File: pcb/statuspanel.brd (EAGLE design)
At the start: 57.1 x 66 mm, 3 parts

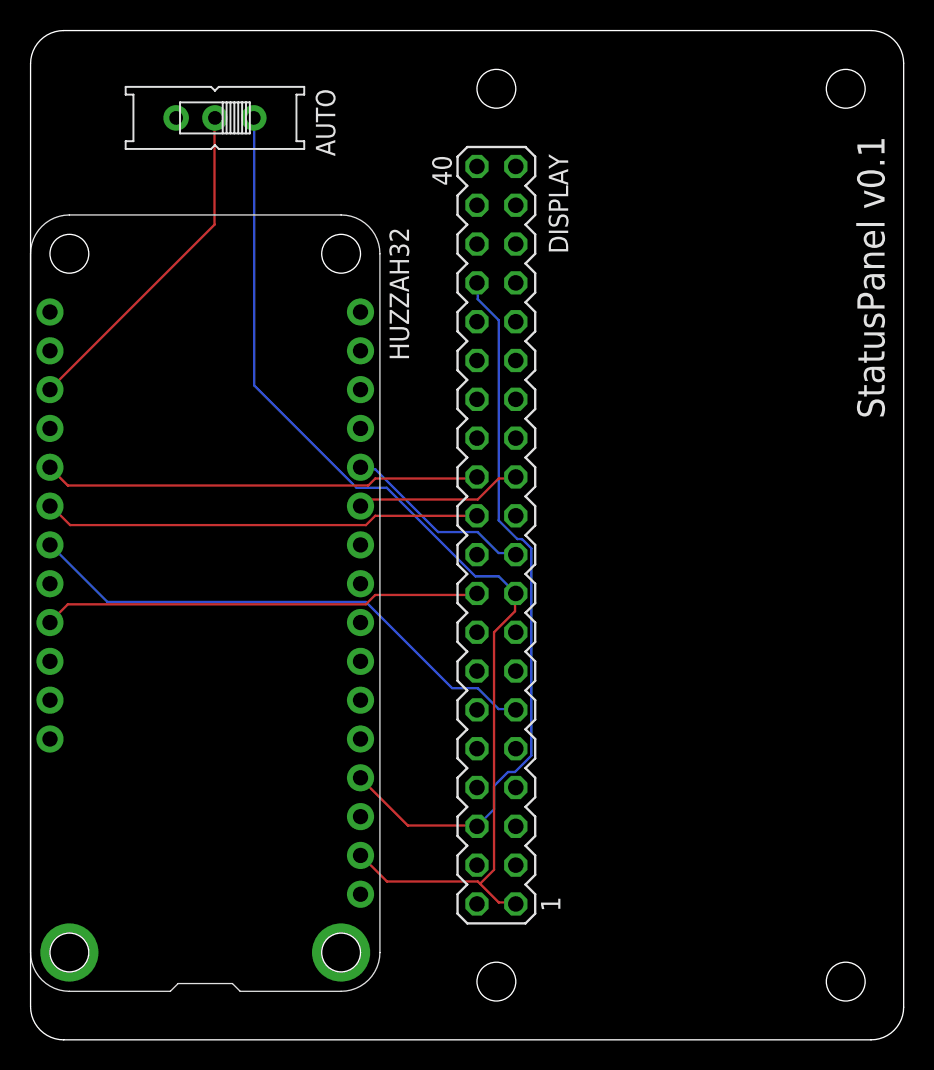
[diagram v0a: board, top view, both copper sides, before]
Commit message: Update the PCB to add an unpair button
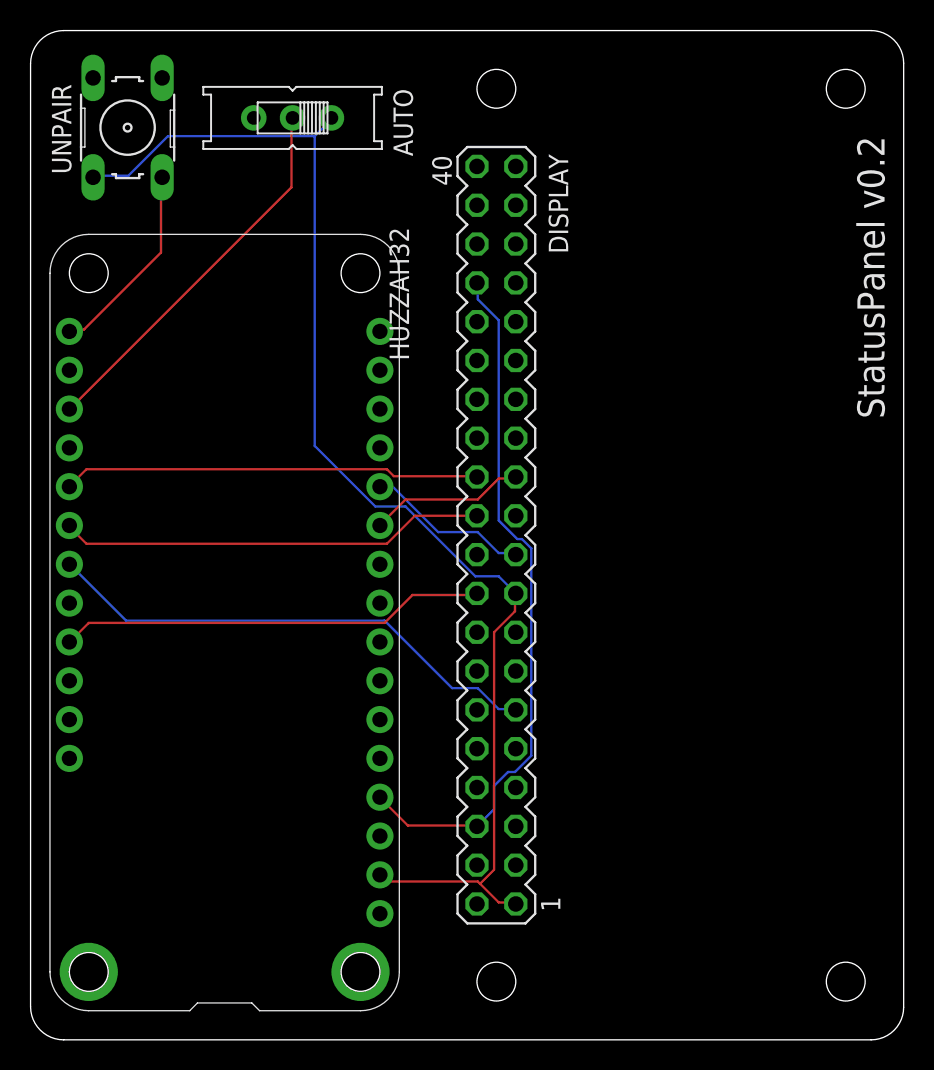
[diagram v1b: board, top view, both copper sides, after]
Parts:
- added UNPAIR: (no value), switch-omron:B3F-10XX
- moved AUTO 5.08 mm to (17.1, 60.3)
- moved HUZZAH32 1.80 mm to (24.1, 1.91)
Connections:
- new net UNPAIR: HUZZAH32.17, UNPAIR.3
- net 3V3: now also UNPAIR.1
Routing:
- net UNPAIR: track 0.00 -> 13.1 mm
- net 3V3: track 71.7 -> 84.5 mm
- net AUTO: track 22.2 -> 25.1 mm
- net RST: track 34.9 -> 33.2 mm
- net GND: track 47.9 -> 46.1 mm
- net MOSI: track 12.6 -> 10.8 mm
- net CS: track 28.7 -> 27.4 mm
- net SCLK: track 11.0 -> 10.2 mm
- net BUSY: track 28.7 -> 28.0 mm
- net DC: track 28.7 -> 28.0 mm
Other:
- board text added: "StatusPanel v0.2"
- board text removed: "StatusPanel v0.1"

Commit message: Rename RST to PANELRESET
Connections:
- net RST renamed PANELRESET
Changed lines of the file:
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@@
 </elements>
 <signals>
-<signal name="RST">
+<signal name="PANELRESET">
 <contactref element="DISPLAY" pad="11"/>
 <contactref element="HUZZAH32" pad="23"/>

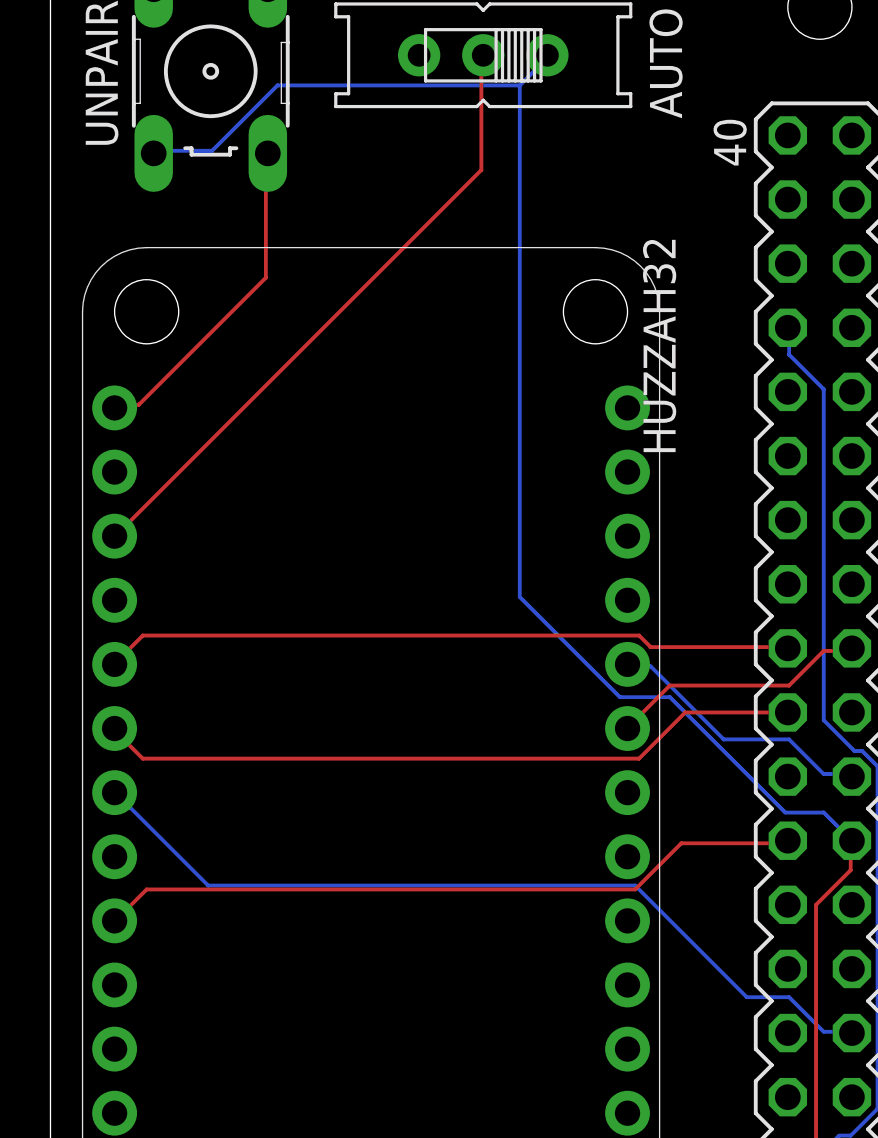
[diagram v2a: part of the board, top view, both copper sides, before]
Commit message: Update the wire for unpair
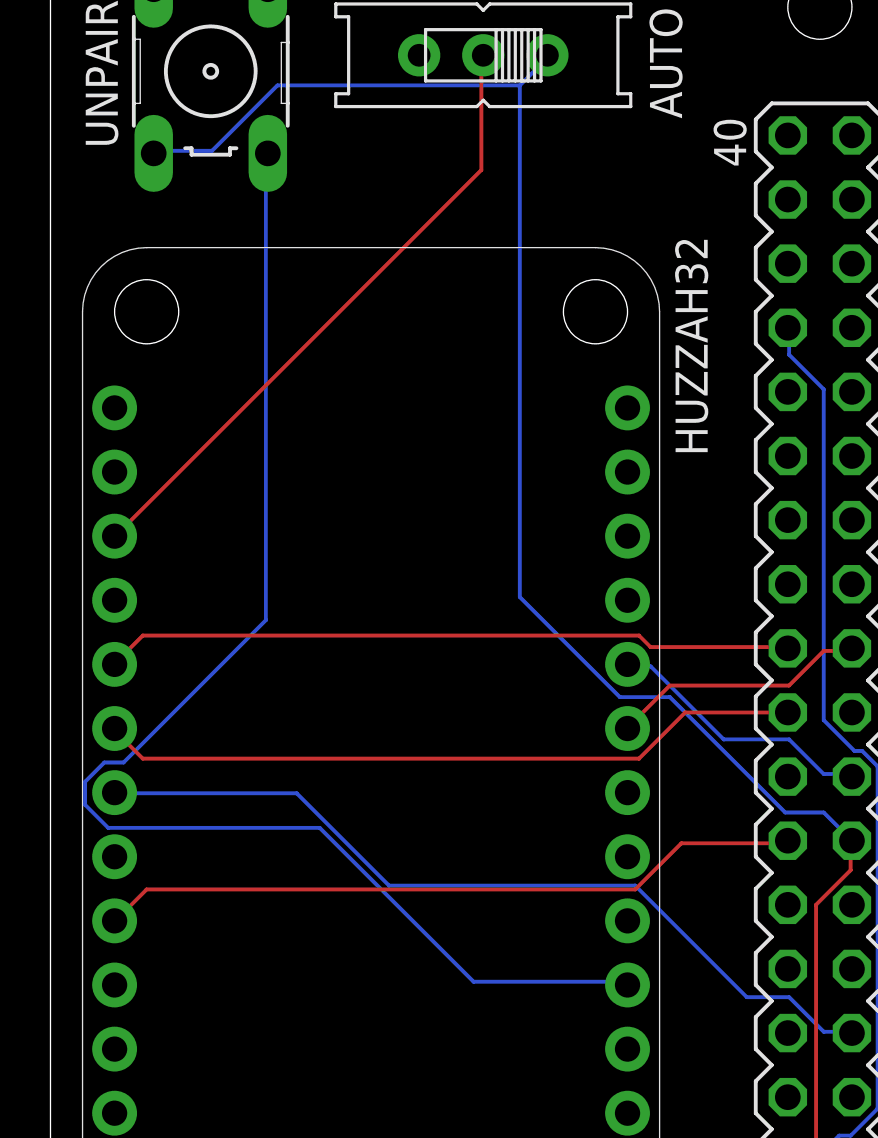
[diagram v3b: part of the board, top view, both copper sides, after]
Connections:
- net UNPAIR: now also HUZZAH32.7; no longer HUZZAH32.17
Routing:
- net UNPAIR: track 13.1 -> 53.8 mm
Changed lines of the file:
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@@
 <hole x="30.48" y="3.81" drill="2.54"/>
 <hole x="30.48" y="62.23" drill="2.54"/>
-<text x="24.765" y="44.45" size="1.27" layer="25" rot="R90">HUZZAH32</text>
+<text x="26.035" y="44.45" size="1.27" layer="25" rot="R90">HUZZAH32</text>
 <hole x="21.59" y="4.445" drill="2.54"/>
 <hole x="3.81" y="4.445" drill="2.54"/>
@@
 <wire x1="27.5844" y1="23.0124" x2="29.2608" y2="23.0124" width="0.1524" layer="16"/>
 <wire x1="23.1648" y1="27.432" x2="27.5844" y2="23.0124" width="0.1524" layer="16"/>
-<wire x1="6.2484" y1="27.432" x2="23.1648" y2="27.432" width="0.1524" layer="16"/>
-<wire x1="2.5908" y1="31.0896" x2="6.2484" y2="27.432" width="0.1524" layer="16"/>
+<wire x1="13.4112" y1="27.432" x2="23.1648" y2="27.432" width="0.1524" layer="16"/>
+<wire x1="9.7536" y1="31.0896" x2="13.4112" y2="27.432" width="0.1524" layer="16"/>
+<wire x1="2.5908" y1="31.0896" x2="9.7536" y2="31.0896" width="0.1524" layer="16"/>
 <wire x1="31.6992" y1="21.6408" x2="31.75" y2="21.59" width="0.1524" layer="16"/>
 <wire x1="2.5908" y1="31.0896" x2="2.54" y2="31.115" width="0.1524" layer="16"/>
@@
 </signal>
 <signal name="UNPAIR">
-<contactref element="HUZZAH32" pad="17"/>
 <contactref element="UNPAIR" pad="3"/>
-<wire x1="8.5344" y1="51.5112" x2="8.5344" y2="56.388" width="0.1524" layer="1"/>
-<wire x1="3.5052" y1="46.482" x2="8.5344" y2="51.5112" width="0.1524" layer="1"/>
-<wire x1="2.5908" y1="46.482" x2="3.5052" y2="46.482" width="0.1524" layer="1"/>
-<wire x1="8.5344" y1="56.388" x2="8.6106" y2="56.4388" width="0.1524" layer="1"/>
-<wire x1="2.5908" y1="46.482" x2="2.54" y2="46.355" width="0.1524" layer="1"/>
+<contactref element="HUZZAH32" pad="7"/>
+<wire x1="8.5344" y1="37.9476" x2="8.5344" y2="56.388" width="0.1524" layer="16"/>
+<wire x1="2.8956" y1="32.3088" x2="8.5344" y2="37.9476" width="0.1524" layer="16"/>
+<wire x1="2.1336" y1="32.3088" x2="2.8956" y2="32.3088" width="0.1524" layer="16"/>
+<wire x1="1.3716" y1="31.5468" x2="2.1336" y2="32.3088" width="0.1524" layer="16"/>
+<wire x1="1.3716" y1="30.6324" x2="1.3716" y2="31.5468" width="0.1524" layer="16"/>
+<wire x1="2.286" y1="29.718" x2="1.3716" y2="30.6324" width="0.1524" layer="16"/>
+<wire x1="10.668" y1="29.718" x2="2.286" y2="29.718" width="0.1524" layer="16"/>
+<wire x1="16.764" y1="23.622" x2="10.668" y2="29.718" width="0.1524" layer="16"/>
+<wire x1="22.86" y1="23.622" x2="16.764" y2="23.622" width="0.1524" layer="16"/>
+<wire x1="8.5344" y1="56.388" x2="8.6106" y2="56.4388" width="0.1524" layer="16"/>
+<wire x1="22.86" y1="23.622" x2="22.86" y2="23.495" width="0.1524" layer="16"/>
 </signal>
 </signals>

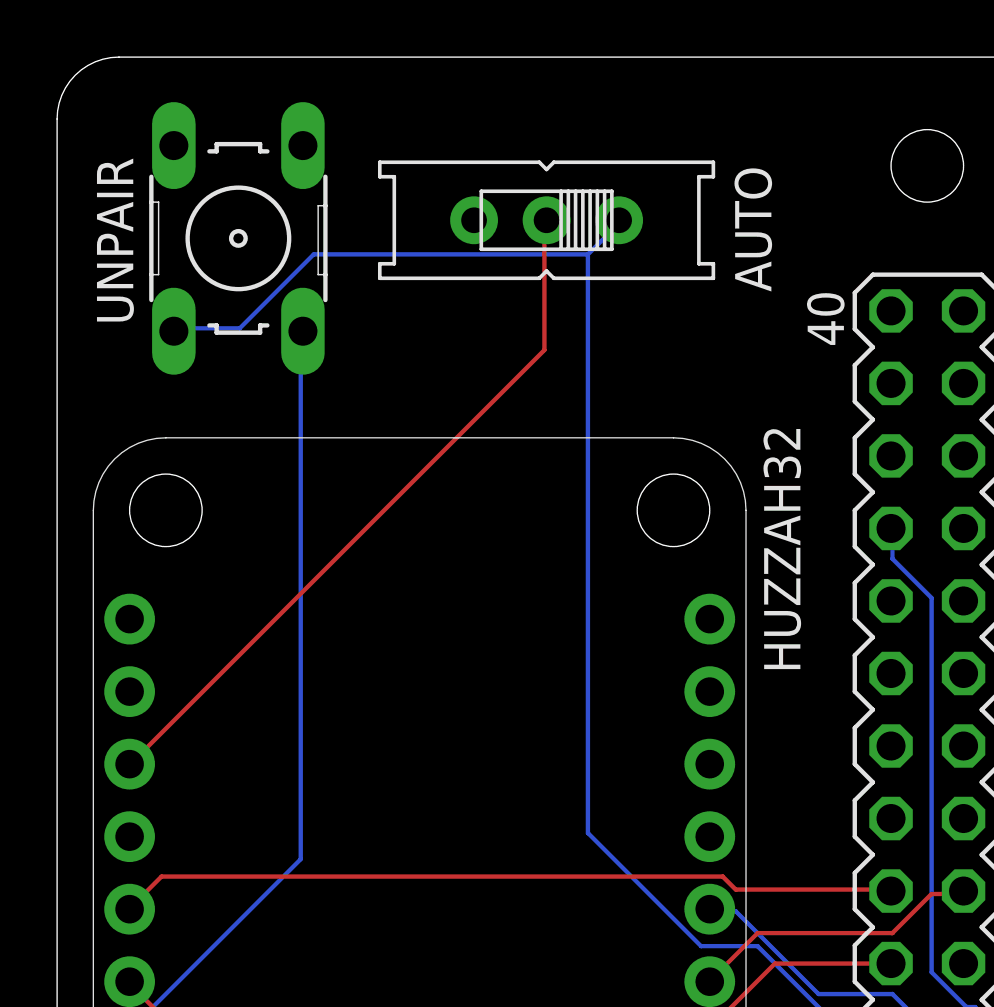
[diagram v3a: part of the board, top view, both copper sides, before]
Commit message: Add an LED
I’m not doing anything with this yet.
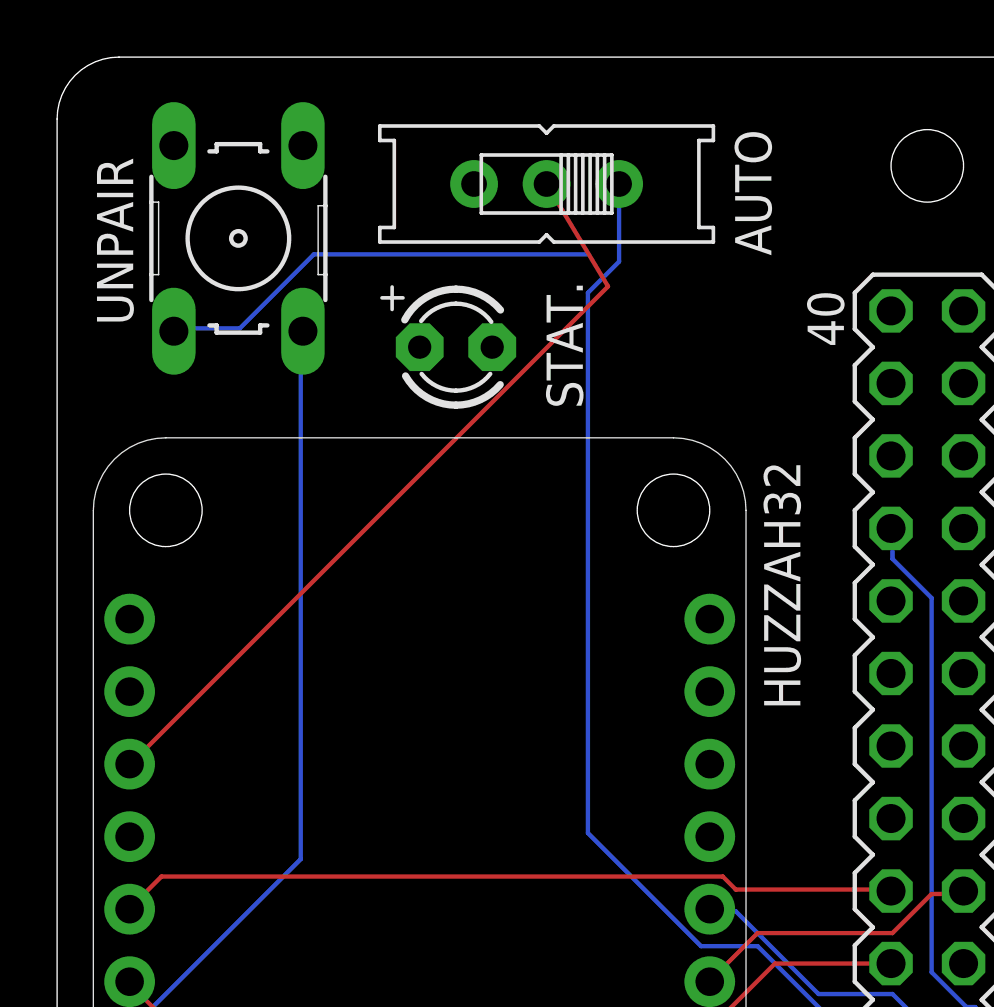
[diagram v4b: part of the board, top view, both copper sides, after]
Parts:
- added STAT.: (no value), adafruit:LED3MM
- moved AUTO 1.27 mm to (17.1, 61.6)
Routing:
- net AUTO: track 25.1 -> 27.9 mm
- net 3V3: track 84.5 -> 85.7 mm
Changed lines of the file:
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@@
 <hole x="30.48" y="3.81" drill="2.54"/>
 <hole x="30.48" y="62.23" drill="2.54"/>
-<text x="26.035" y="44.45" size="1.27" layer="25" rot="R90">HUZZAH32</text>
+<text x="26.035" y="43.18" size="1.27" layer="25" rot="R90">HUZZAH32</text>
 <hole x="21.59" y="4.445" drill="2.54"/>
 <hole x="3.81" y="4.445" drill="2.54"/>
@@
 </element>
 <element name="HUZZAH32" library="adafruit" library_urn="urn:adsk.eagle:library:420" package="FEATHERWING_DIM" value="FEATHERWING_NODIM" x="24.13" y="1.905" smashed="yes" rot="R90"/>
-<element name="AUTO" library="adafruit" library_urn="urn:adsk.eagle:library:420" package="EG1218" package3d_urn="urn:adsk.eagle:package:6240649/1" value="" x="17.145" y="60.325" smashed="yes" rot="R180">
-<attribute name="NAME" x="23.749" y="62.23" size="1.27" layer="25" font="vector" rot="R270"/>
+<element name="AUTO" library="adafruit" library_urn="urn:adsk.eagle:library:420" package="EG1218" package3d_urn="urn:adsk.eagle:package:6240649/1" value="" x="17.145" y="61.595" smashed="yes" rot="R180">
+<attribute name="NAME" x="23.749" y="63.5" size="1.27" layer="25" font="vector" rot="R270"/>
 </element>
 <element name="UNPAIR" library="switch-omron" library_urn="urn:adsk.eagle:library:377" package="B3F-10XX" package3d_urn="urn:adsk.eagle:package:27496/1" value="" x="6.35" y="59.69" smashed="yes" rot="R90">
@@
 <attribute name="POPULARITY" value="72" x="6.35" y="59.69" size="1.778" layer="27" rot="R90" display="off"/>
 <attribute name="VALUE" x="11.43" y="56.642" size="1.27" layer="27" ratio="10" rot="R90"/>
+</element>
+<element name="STAT." library="adafruit" library_urn="urn:adsk.eagle:library:420" package="LED3MM" package3d_urn="urn:adsk.eagle:package:6240537/1" value="" x="13.97" y="55.88" smashed="yes">
+<attribute name="NAME" x="18.415" y="53.721" size="1.27" layer="25" ratio="10" rot="R90"/>
+<attribute name="VALUE" x="15.875" y="54.229" size="1.27" layer="27" ratio="10"/>
 </element>
 </elements>
@@
 <wire x1="8.9916" y1="59.1312" x2="6.4008" y2="56.5404" width="0.1524" layer="16"/>
 <wire x1="18.5928" y1="59.1312" x2="8.9916" y2="59.1312" width="0.1524" layer="16"/>
-<wire x1="19.6596" y1="60.198" x2="18.5928" y2="59.1312" width="0.1524" layer="16"/>
 <wire x1="4.1148" y1="56.5404" x2="4.0894" y2="56.4388" width="0.1524" layer="16"/>
-<wire x1="19.6596" y1="60.198" x2="19.685" y2="60.325" width="0.1524" layer="16"/>
+<wire x1="19.685" y1="61.595" x2="19.685" y2="58.8772" width="0.1524" layer="16"/>
+<wire x1="19.685" y1="58.8772" x2="18.5928" y2="57.785" width="0.1524" layer="16"/>
 <wire x1="30.6324" y1="8.9916" x2="31.6992" y2="8.9916" width="0.1524" layer="1"/>
 <wire x1="29.2608" y1="10.3632" x2="29.4132" y2="10.2108" width="0.1524" layer="1"/>
@@
 <wire x1="29.4132" y1="10.2108" x2="30.3276" y2="11.1252" width="0.1524" layer="1"/>
 <wire x1="31.6992" y1="29.1084" x2="31.75" y2="29.21" width="0.1524" layer="1"/>
-<wire x1="18.5928" y1="38.862" x2="18.5928" y2="59.1312" width="0.1524" layer="16"/>
+<wire x1="18.5928" y1="38.862" x2="18.5928" y2="57.785" width="0.1524" layer="16"/>
 <wire x1="22.5552" y1="34.8996" x2="18.5928" y2="38.862" width="0.1524" layer="16"/>
 <wire x1="24.5364" y1="34.8996" x2="22.5552" y2="34.8996" width="0.1524" layer="16"/>
@@
 <contactref element="HUZZAH32" pad="19"/>
 <contactref element="AUTO" pad="P"/>
-<wire x1="17.0688" y1="55.7784" x2="17.0688" y2="60.198" width="0.1524" layer="1"/>
-<wire x1="2.5908" y1="41.3004" x2="17.0688" y2="55.7784" width="0.1524" layer="1"/>
-<wire x1="17.0688" y1="60.198" x2="17.145" y2="60.325" width="0.1524" layer="1"/>
+<wire x1="2.5908" y1="41.3004" x2="19.29765" y2="58.00725" width="0.1524" layer="1"/>
+<wire x1="19.29765" y1="58.00725" x2="17.145" y2="61.595" width="0.1524" layer="1"/>
 <wire x1="2.5908" y1="41.3004" x2="2.54" y2="41.275" width="0.1524" layer="1"/>
 </signal>
